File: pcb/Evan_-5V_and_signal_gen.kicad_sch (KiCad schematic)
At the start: 19 parts, among them IC1 TL7660IDGKR, IC2 TL081IDT

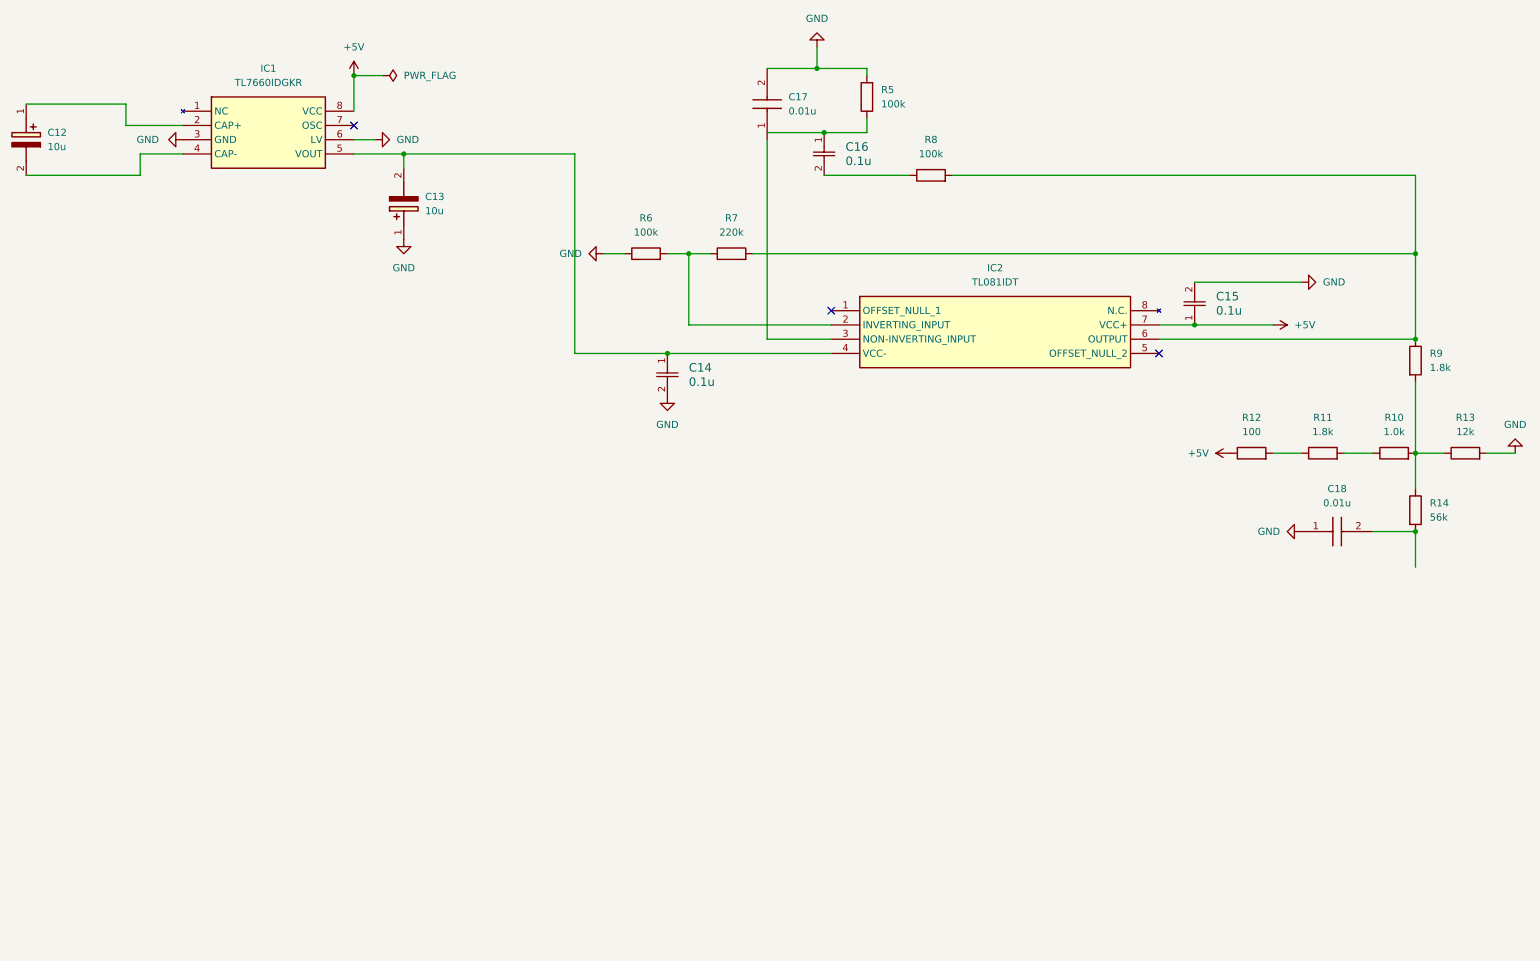
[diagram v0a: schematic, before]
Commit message: Evan---Adding_PC104_Connector
Added the PC104 connector, added global -5v and signal output labels, changed r12 to 330, and added r21 of 150k.
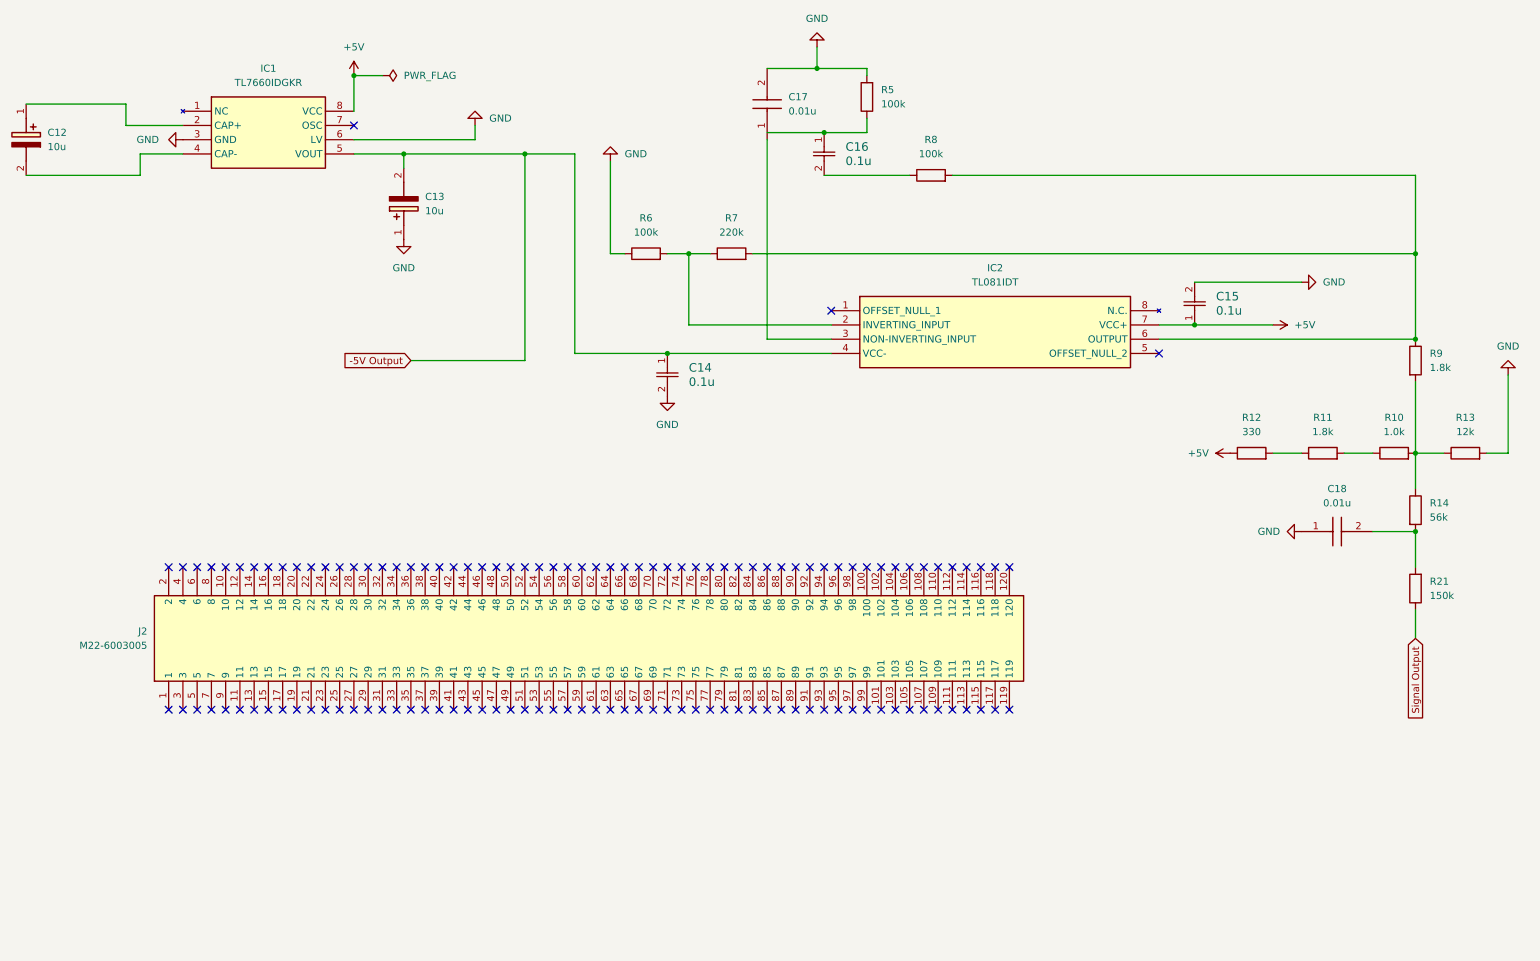
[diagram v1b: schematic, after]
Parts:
- added J2: M22-6003005, RHDR120W55P200_4X30_6020X800X935P, symbol capstone:M22-6003005
- added R21: 150k, Resistor_SMD:R_0402_1005Metric, symbol Device:R
- C14, C15, C16: footprint CAPC220145_88N_KEM -> capstone:CAPC220145_88N_KEM-0.1u
- R12: value 100 -> 330
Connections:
- net -5V Output: now reaches C13.2 (-), C14.1, IC1.5 (VOUT), IC2.4 (VCC-)
- net at C18.2, R14.2: now also R21.2
- new net Signal Output: R21.1
- no-connect marks 3 -> 123

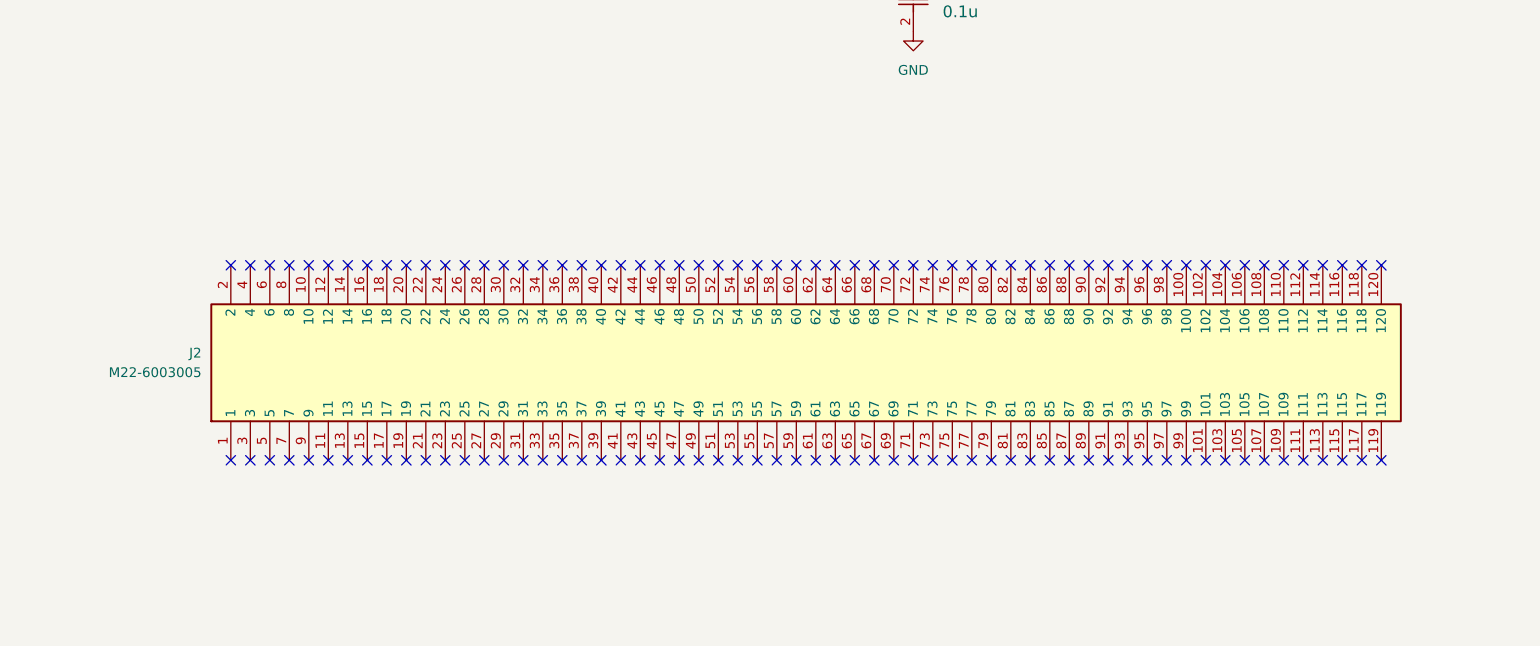
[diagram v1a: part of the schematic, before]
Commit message: Adding 3.3v reg
added 3.3v regulator circuit.
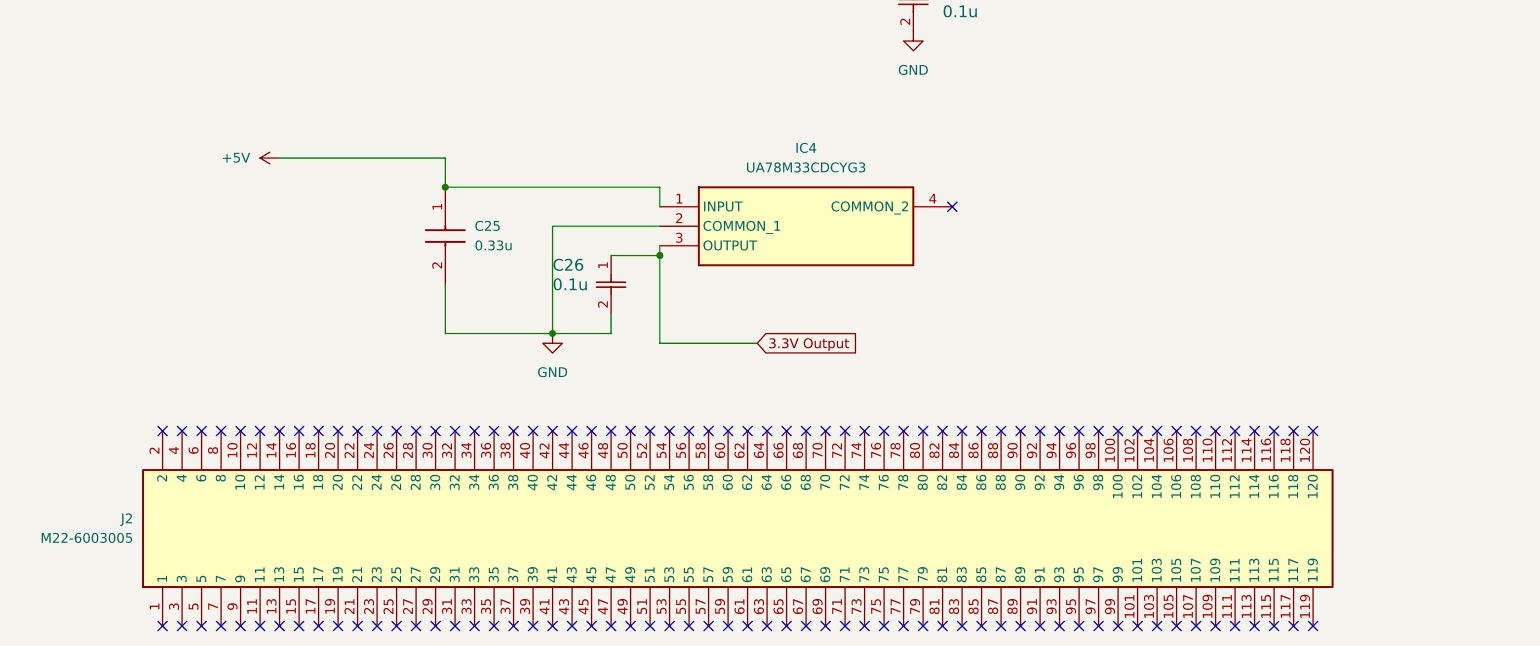
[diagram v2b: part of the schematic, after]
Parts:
- added C25: 0.33u, C0805, symbol capstone:C0805C334K3RACAUTO7210
- added C26: 0.1u, capstone:CAPC220145_88N_KEM-0.1u, symbol capstone:C0805C104K5RAC7210
- added IC4: UA78M33CDCYG3, SOT230P700X180-4N, symbol capstone:UA78M33CDCYG3
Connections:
- net +5V: now also C25.1, IC4.1 (INPUT)
- net GND: now also C25.2, C26.2, IC4.2 (COMMON_1)
- new net 3.3V Output: C26.1, IC4.3 (OUTPUT)
- no-connect marks 123 -> 124
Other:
- moved on the sheet: J2
